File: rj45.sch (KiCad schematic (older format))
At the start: 3 parts

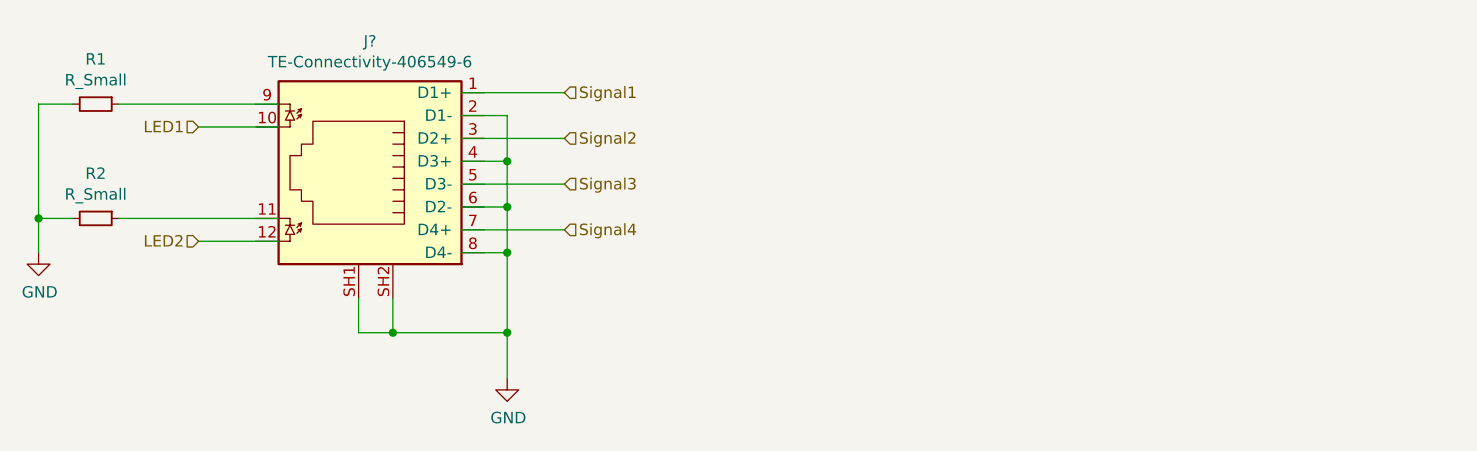
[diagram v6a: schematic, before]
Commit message: Began redesigning with Si8660
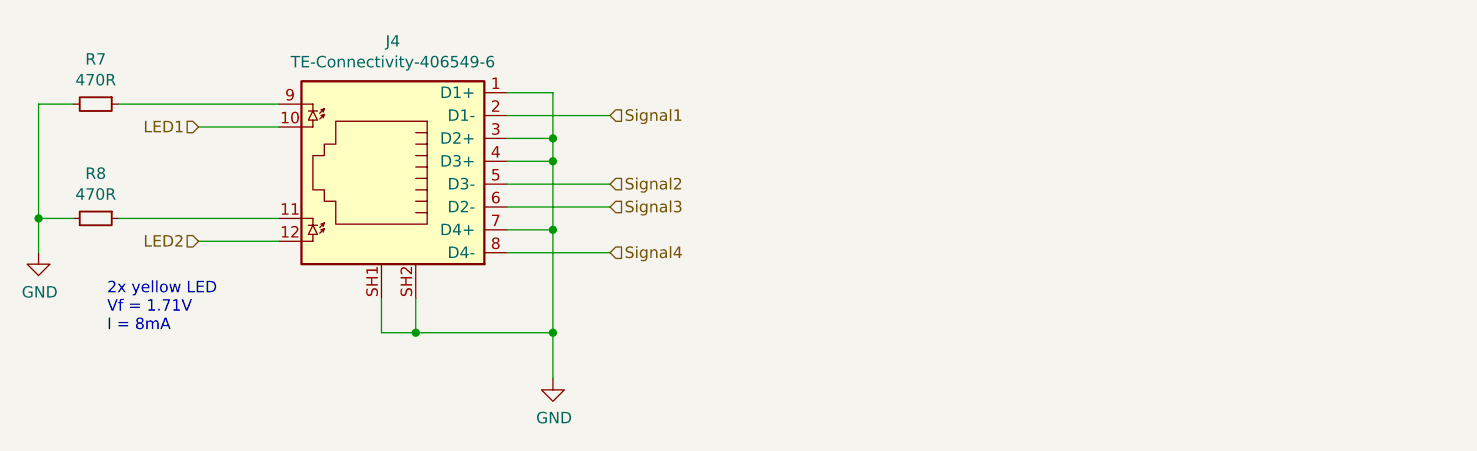
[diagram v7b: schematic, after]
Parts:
- J2: renamed from J?; footprint (none) -> Matthias:TE-Connectivity-406549-6
- R1, R2: value R_Small -> 470R
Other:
- note added: "2x yellow LED\nVf = 1.71V\nI = 8mA"
- moved on the sheet: J4
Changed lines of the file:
@@
 Comment4 ""
 $EndDescr
-Wire Wire Line
-	6900 3800 6700 3800
-Wire Wire Line
-	6700 4000 6900 4000
-Connection ~ 6900 4000
-Wire Wire Line
-	6900 4000 6900 3800
-Wire Wire Line
-	6700 4200 6900 4200
-Connection ~ 6900 4200
-Wire Wire Line
-	6900 4200 6900 4000
-Wire Wire Line
-	6700 4400 6900 4400
-Connection ~ 6900 4400
-Wire Wire Line
-	6900 4400 6900 4200
-Text HLabel 7150 3700 2    50   Input ~ 0
+Text HLabel 7350 3800 2    50   Input ~ 0
 Signal1
-Text HLabel 7150 3900 2    50   Input ~ 0
+Text HLabel 7350 4100 2    50   Input ~ 0
 Signal2
-Text HLabel 7150 4100 2    50   Input ~ 0
+Text HLabel 7350 4200 2    50   Input ~ 0
 Signal3
-Text HLabel 7150 4300 2    50   Input ~ 0
+Text HLabel 7350 4400 2    50   Input ~ 0
 Signal4
 Wire Wire Line
-	7150 4300 6700 4300
+	7350 4400 6900 4400
 Wire Wire Line
-	7150 4100 6700 4100
+	7350 4200 6900 4200
 Wire Wire Line
-	7150 3900 6700 3900
+	7350 4100 6900 4100
 Wire Wire Line
-	7150 3700 6700 3700
+	7350 3800 6900 3800
 $Comp
-L power:GND #PWR044
+L power:GND #PWR033
 U 1 1 5BCF77E9
-P 6900 4950
-AR Path="/5BCCA241/5BCF77E9" Ref="#PWR044"  Part="1"
-AR Path="/5BCCB065/5BCF77E9" Ref="#PWR047"  Part="1"
-AR Path="/5BCCB3D0/5BCF77E9" Ref="#PWR050"  Part="1"
-AR Path="/5BCCB87F/5BCF77E9" Ref="#PWR053"  Part="1"
-F 0 "#PWR044" H 6900 4700 50  0001 C CNN
-F 1 "GND" H 6905 4777 50  0000 C CNN
-F 2 "" H 6900 4950 50  0001 C CNN
-F 3 "" H 6900 4950 50  0001 C CNN
-	1    6900 4950
+P 7100 4950
+AR Path="/5BCCA241/5BCF77E9" Ref="#PWR033"  Part="1"
+AR Path="/5BCCB065/5BCF77E9" Ref="#PWR035"  Part="1"
+AR Path="/5BCCB3D0/5BCF77E9" Ref="#PWR037"  Part="1"
+AR Path="/5BCCB87F/5BCF77E9" Ref="#PWR039"  Part="1"
+F 0 "#PWR039" H 7100 4700 50  0001 C CNN
+F 1 "GND" H 7105 4777 50  0000 C CNN
+F 2 "" H 7100 4950 50  0001 C CNN
+F 3 "" H 7100 4950 50  0001 C CNN
+	1    7100 4950
 	1    0    0    -1
 $EndComp
@@
 Text HLabel 5550 4350 0    50   Input ~ 0
 LED2
+Connection ~ 7100 4750
 Wire Wire Line
-	6900 4400 6900 4750
-Wire Wire Line
-	6250 4600 6250 4750
-Wire Wire Line
-	6250 4750 6400 4750
-Connection ~ 6900 4750
-Wire Wire Line
-	6900 4750 6900 4950
-Wire Wire Line
-	6400 4600 6400 4750
-Connection ~ 6400 4750
-Wire Wire Line
-	6400 4750 6900 4750
+	7100 4750 7100 4950
 Wire Wire Line
 	5900 4350 5550 4350
@@
 AR Path="/5BCCB065/5BE0DDBF" Ref="R3"  Part="1"
 AR Path="/5BCCB87F/5BE0DDBF" Ref="R7"  Part="1"
-F 0 "R1" V 4904 3750 50  0000 C CNN
-F 1 "R_Small" V 4995 3750 50  0000 C CNN
+F 0 "R7" V 4904 3750 50  0000 C CNN
+F 1 "470R" V 4995 3750 50  0000 C CNN
 F 2 "Resistor_SMD:R_0805_2012Metric_Pad1.15x1.40mm_HandSolder" H 5100 3750 50  0001 C CNN
 F 3 "~" H 5100 3750 50  0001 C CNN
@@
 AR Path="/5BCCB065/5BE0E685" Ref="R4"  Part="1"
 AR Path="/5BCCB87F/5BE0E685" Ref="R8"  Part="1"
-F 0 "R2" V 4904 4250 50  0000 C CNN
-F 1 "R_Small" V 4995 4250 50  0000 C CNN
+F 0 "R8" V 4904 4250 50  0000 C CNN
+F 1 "470R" V 4995 4250 50  0000 C CNN
 F 2 "Resistor_SMD:R_0805_2012Metric_Pad1.15x1.40mm_HandSolder" H 5100 4250 50  0001 C CNN
 F 3 "~" H 5100 4250 50  0001 C CNN
@@
 	5200 4250 5900 4250
 $Comp
-L power:GND #PWR043
+L power:GND #PWR032
 U 1 1 5BE0E68D
 P 4850 4400
-AR Path="/5BCCA241/5BE0E68D" Ref="#PWR043"  Part="1"
-AR Path="/5BCCB065/5BE0E68D" Ref="#PWR046"  Part="1"
-AR Path="/5BCCB3D0/5BE0E68D" Ref="#PWR049"  Part="1"
-AR Path="/5BCCB87F/5BE0E68D" Ref="#PWR052"  Part="1"
-F 0 "#PWR043" H 4850 4150 50  0001 C CNN
+AR Path="/5BCCA241/5BE0E68D" Ref="#PWR032"  Part="1"
+AR Path="/5BCCB065/5BE0E68D" Ref="#PWR034"  Part="1"
+AR Path="/5BCCB3D0/5BE0E68D" Ref="#PWR036"  Part="1"
+AR Path="/5BCCB87F/5BE0E68D" Ref="#PWR038"  Part="1"
+F 0 "#PWR038" H 4850 4150 50  0001 C CNN
 F 1 "GND" H 4855 4227 50  0000 C CNN
 F 2 "" H 4850 4400 50  0001 C CNN
@@
 $EndComp
 $Comp
-L Matthias:TE-Connectivity-406549-6 J?
+L Matthias:TE-Connectivity-406549-6 J2
 U 1 1 5BE18A0E
-P 6300 4100
-F 0 "J?" H 6300 4725 50  0000 C CNN
-F 1 "TE-Connectivity-406549-6" H 6300 4634 50  0000 C CNN
-F 2 "" V 6300 4175 50  0001 C CNN
-F 3 "~" V 6300 4175 50  0001 C CNN
-	1    6300 4100
+P 6400 4100
+AR Path="/5BCCB065/5BE18A0E" Ref="J2"  Part="1"
+AR Path="/5BCCA241/5BE18A0E" Ref="J1"  Part="1"
+AR Path="/5BCCB3D0/5BE18A0E" Ref="J3"  Part="1"
+AR Path="/5BCCB87F/5BE18A0E" Ref="J4"  Part="1"
+F 0 "J4" H 6400 4725 50  0000 C CNN
+F 1 "TE-Connectivity-406549-6" H 6400 4634 50  0000 C CNN
+F 2 "Matthias:TE-Connectivity-406549-6" V 6400 4175 50  0001 C CNN
+F 3 "~" V 6400 4175 50  0001 C CNN
+	1    6400 4100
 	1    0    0    -1
 $EndComp
@@
 Wire Wire Line
 	4850 4250 4850 4400
+Text Notes 5150 4750 0    50   ~ 0
+2x yellow LED\nVf = 1.71V\nI = 8mA
+Wire Wire Line
+	6350 4750 6350 4600
+Wire Wire Line
+	6350 4750 6500 4750
+Wire Wire Line
+	6500 4600 6500 4750
+Connection ~ 6500 4750
+Wire Wire Line
+	6500 4750 7100 4750
+Wire Wire Line
+	7100 3700 6900 3700
+Wire Wire Line
+	7100 3700 7100 3900
+Wire Wire Line
+	6900 3900 7100 3900
+Connection ~ 7100 3900
+Wire Wire Line
+	7100 3900 7100 4000
+Wire Wire Line
+	6900 4000 7100 4000
+Connection ~ 7100 4000
+Wire Wire Line
+	7100 4000 7100 4300
+Wire Wire Line
+	6900 4300 7100 4300
+Connection ~ 7100 4300
+Wire Wire Line
+	7100 4300 7100 4750
 $EndSCHEMATC

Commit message: Finished layout with 4x Si8660
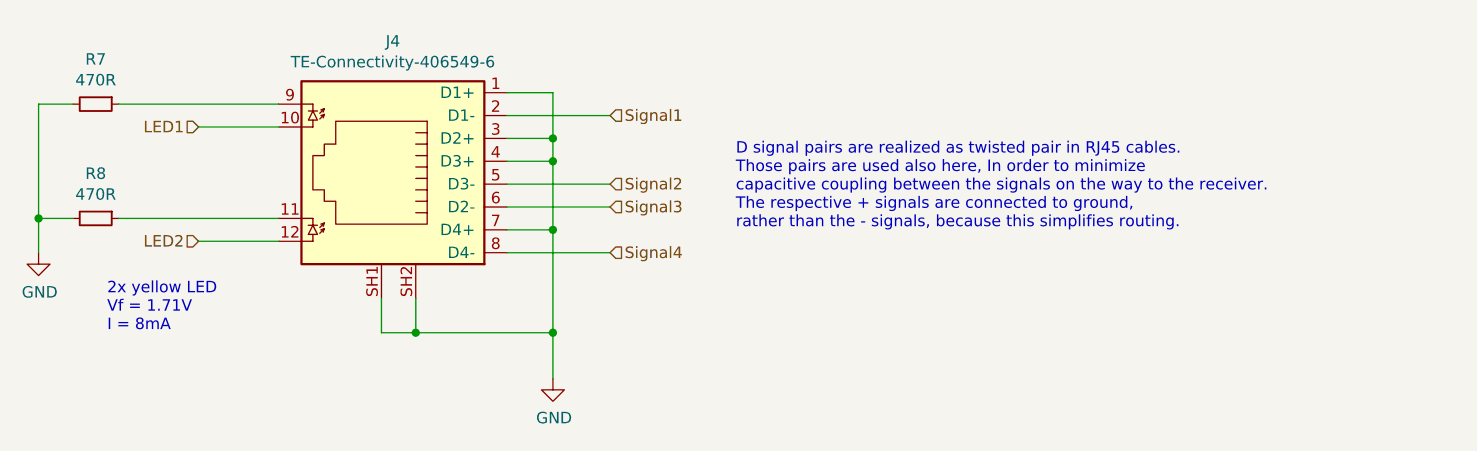
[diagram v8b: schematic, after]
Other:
- note added: "D signal pairs are realized as twisted pair in RJ45 cables.\nThose pairs are used also here, In order to minimize\ncapacitive coupling between the signals on the way to the receiver.\nThe respective + signals are connected to ground,\nrather than the - signals, because this simplifies routing."
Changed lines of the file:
@@
 $Descr A4 11693 8268
 encoding utf-8
-Sheet 8 11
+Sheet 5 11
 Title ""
 Date ""
@@
 Wire Wire Line
 	7100 4300 7100 4750
+Text Notes 7900 4300 0    50   ~ 0
+D signal pairs are realized as twisted pair in RJ45 cables.\nThose pairs are used also here, In order to minimize\ncapacitive coupling between the signals on the way to the receiver.\nThe respective + signals are connected to ground,\nrather than the - signals, because this simplifies routing.
 $EndSCHEMATC
